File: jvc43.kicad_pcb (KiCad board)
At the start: 6 copper layers, 101.6 x 50.8 mm, 140 parts, among them J201 8P8C_LED_Shielded, J301 8P8C_LED_Shielded, J401 USB_C_Receptacle_USB2.0, U201 LAN8831, U301 LAN8831, U401 LTC3622*DE, X101 25 MHz

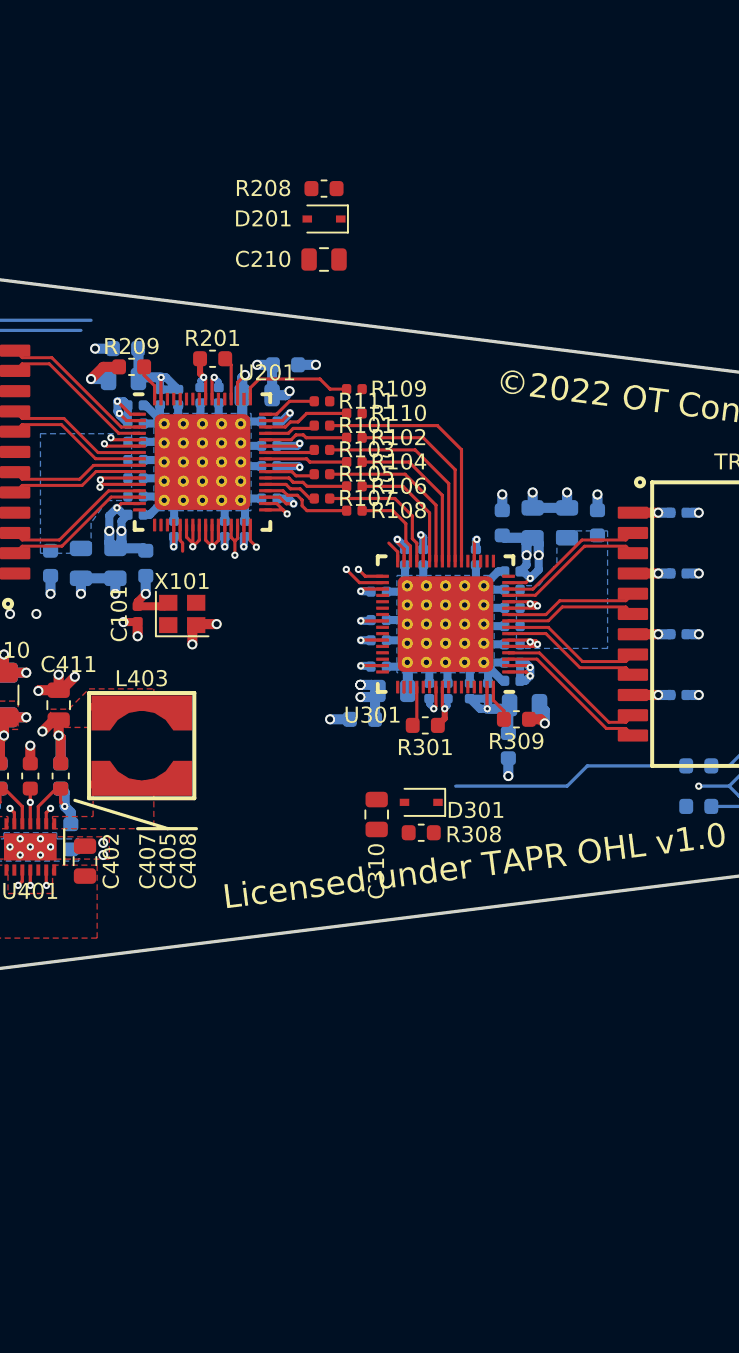
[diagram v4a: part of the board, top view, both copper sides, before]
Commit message: Added the absurd number of config/MODE/PHYAD strap resistors, 16 per PHY !!! They have been added to the layout, but not yet placed or routed.
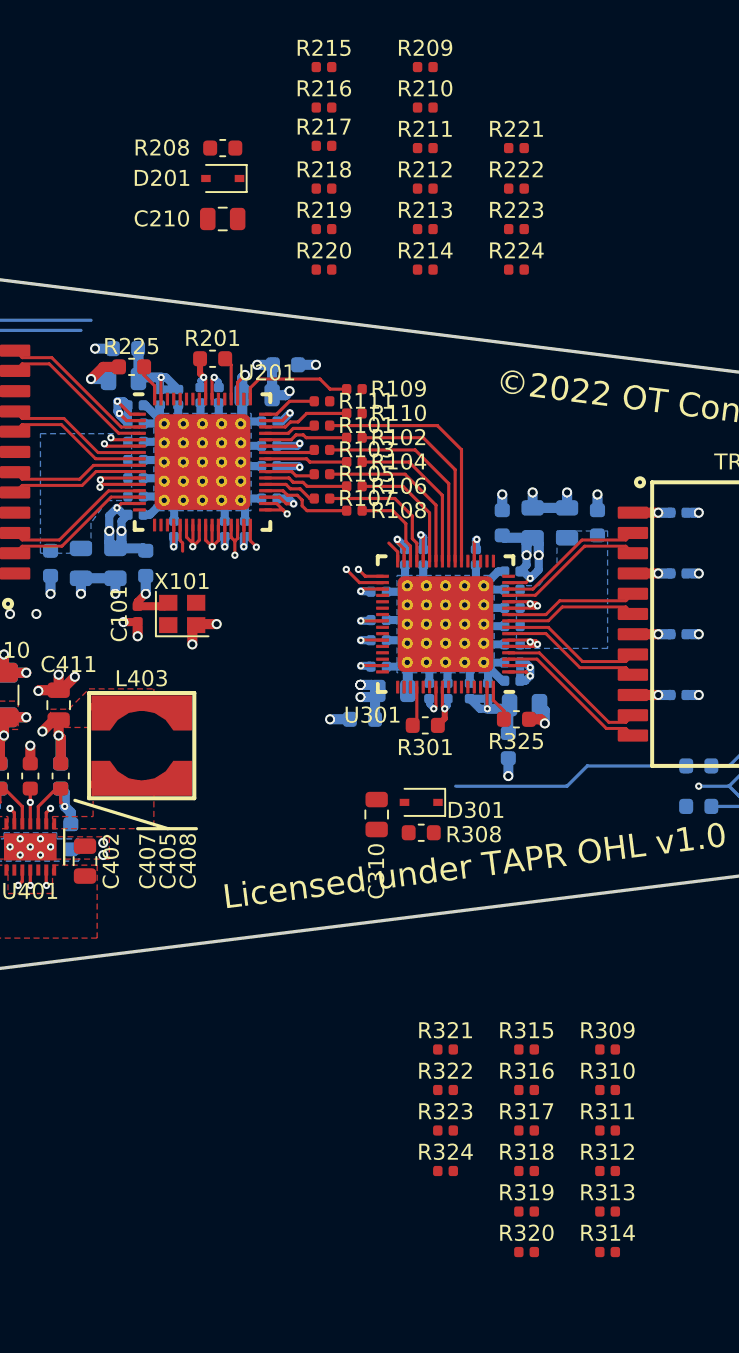
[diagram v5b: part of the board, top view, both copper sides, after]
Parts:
- added R209: 10k, Resistor_SMD:R_0402_1005Metric, F.Cu at (82.5, 15.9)
- added R210: 10k, Resistor_SMD:R_0402_1005Metric, F.Cu at (82.5, 18.4)
- added R211: 10k, Resistor_SMD:R_0402_1005Metric, F.Cu at (82.5, 21.0)
- added R212: 10k, Resistor_SMD:R_0402_1005Metric, F.Cu at (82.5, 23.5)
- added R213: 10k, Resistor_SMD:R_0402_1005Metric, F.Cu at (82.5, 26.0)
- added R214: 10k, Resistor_SMD:R_0402_1005Metric, F.Cu at (82.5, 28.6)
- added R215: 10k, Resistor_SMD:R_0402_1005Metric, F.Cu at (76.2, 15.9)
- added R216: 10k, Resistor_SMD:R_0402_1005Metric, F.Cu at (76.2, 18.4)
- added R217: dnp, Resistor_SMD:R_0402_1005Metric, F.Cu at (76.2, 20.8)
- added R218: 10k, Resistor_SMD:R_0402_1005Metric, F.Cu at (76.2, 23.5)
- added R219: 10k, Resistor_SMD:R_0402_1005Metric, F.Cu at (76.2, 26.0)
- added R220: 10k, Resistor_SMD:R_0402_1005Metric, F.Cu at (76.2, 28.6)
- added R221: 10k, Resistor_SMD:R_0402_1005Metric, F.Cu at (88.3, 21.0)
- added R222: 10k, Resistor_SMD:R_0402_1005Metric, F.Cu at (88.3, 23.5)
- added R223: 10k, Resistor_SMD:R_0402_1005Metric, F.Cu at (88.3, 26.0)
- added R224: 10k, Resistor_SMD:R_0402_1005Metric, F.Cu at (88.3, 28.6)
- added R309: 10k, Resistor_SMD:R_0402_1005Metric, F.Cu at (94.0, 77.5)
- added R310: 10k, Resistor_SMD:R_0402_1005Metric, F.Cu at (94.0, 80.0)
- added R311: 10k, Resistor_SMD:R_0402_1005Metric, F.Cu at (94.0, 82.5)
- added R312: 10k, Resistor_SMD:R_0402_1005Metric, F.Cu at (94.0, 85.1)
- added R313: 10k, Resistor_SMD:R_0402_1005Metric, F.Cu at (94.0, 87.6)
- added R314: 10k, Resistor_SMD:R_0402_1005Metric, F.Cu at (94.0, 90.2)
- added R315: 10k, Resistor_SMD:R_0402_1005Metric, F.Cu at (88.9, 77.5)
- added R316: 10k, Resistor_SMD:R_0402_1005Metric, F.Cu at (88.9, 80.0)
- added R317: dnp, Resistor_SMD:R_0402_1005Metric, F.Cu at (88.9, 82.5)
- added R318: 10k, Resistor_SMD:R_0402_1005Metric, F.Cu at (88.9, 85.1)
- added R319: 10k, Resistor_SMD:R_0402_1005Metric, F.Cu at (88.9, 87.6)
- added R320: 10k, Resistor_SMD:R_0402_1005Metric, F.Cu at (88.9, 90.2)
- added R321: 10k, Resistor_SMD:R_0402_1005Metric, F.Cu at (83.8, 77.5)
- added R322: 10k, Resistor_SMD:R_0402_1005Metric, F.Cu at (83.8, 80.0)
- added R323: 10k, Resistor_SMD:R_0402_1005Metric, F.Cu at (83.8, 82.5)
- added R324: 10k, Resistor_SMD:R_0402_1005Metric, F.Cu at (83.8, 85.1)
- R202, R203, R302, R303: value 100 -> 220
- moved C210 6.84 mm to (69.8, 25.4)
- moved R208 6.84 mm to (69.8, 21.0)
- moved D201 6.84 mm to (69.8, 22.9)
- renumbered R209 to R225, R309 to R325
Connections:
- J201 pad 10: GND -> /Ethernet1/green
- J201 pad 11: /Ethernet1/yellow -> +2V5
- J201 pad 12: GND -> /Ethernet1/yellow
- J201 pad 9: /Ethernet1/green -> +2V5
- J301 pad 10: GND -> /Ethernet2/green
- J301 pad 11: /Ethernet2/yellow -> +2V5
- J301 pad 12: GND -> /Ethernet2/yellow
- J301 pad 9: /Ethernet2/green -> +2V5
- R202 pad 1: /Ethernet1/100_LED -> /Ethernet1/LED1
- R203 pad 1: /Ethernet1/1000_LED -> /Ethernet1/LED2
- R302 pad 1: /Ethernet2/100_LED -> /Ethernet2/LED1
- R303 pad 1: /Ethernet2/1000_LED -> /Ethernet2/LED2
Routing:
- net /Ethernet2/LED1: track 0.00 -> 15.0 mm
- net /Ethernet2/100_LED: track 15.0 -> 0.00 mm
- net /Ethernet1/LED2: track 0.00 -> 13.7 mm
- net /Ethernet1/1000_LED: track 13.7 -> 0.00 mm
- net /Ethernet1/LED1: track 1.70 -> 14.5 mm
- net /Ethernet1/100_LED: track 12.8 -> 0.00 mm

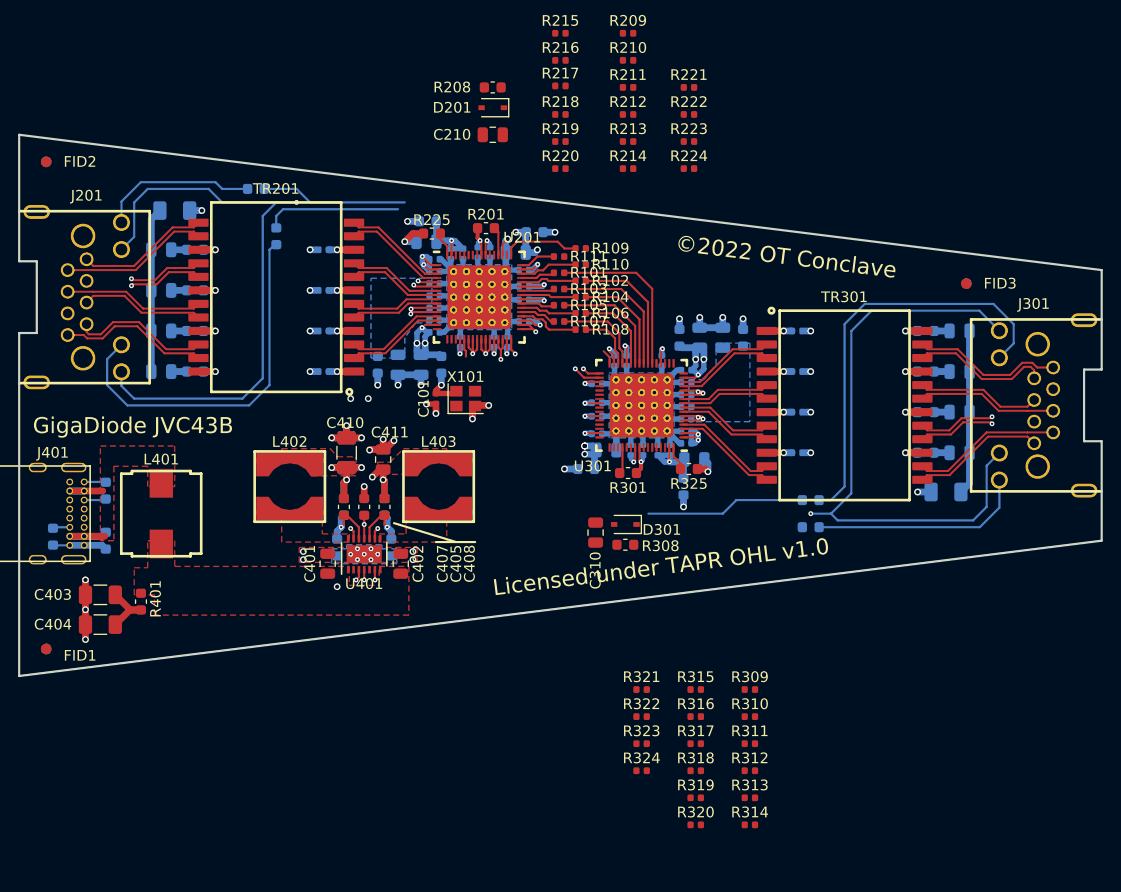
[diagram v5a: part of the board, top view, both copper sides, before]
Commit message: - Fixed a schematic bug, one of the strap resistors was connected to RXD2 but   should have been RXD4 - Swapped out reset 10k resistor from size 0603 to size 0402, since I have now   32 more of them in the smaller size... also assigned a mfr P/N to all those - Placed and routed *EVERYTHING* for PHY2, mainly all the new strap resistors - Placed and routed the new LED traces (both PHYs), and a few of the PHY1   straps, namely the LED1-5 straps
Still to go: place & route of the config & PHYAD strap resistors for PHY1...
It's getting very crowded
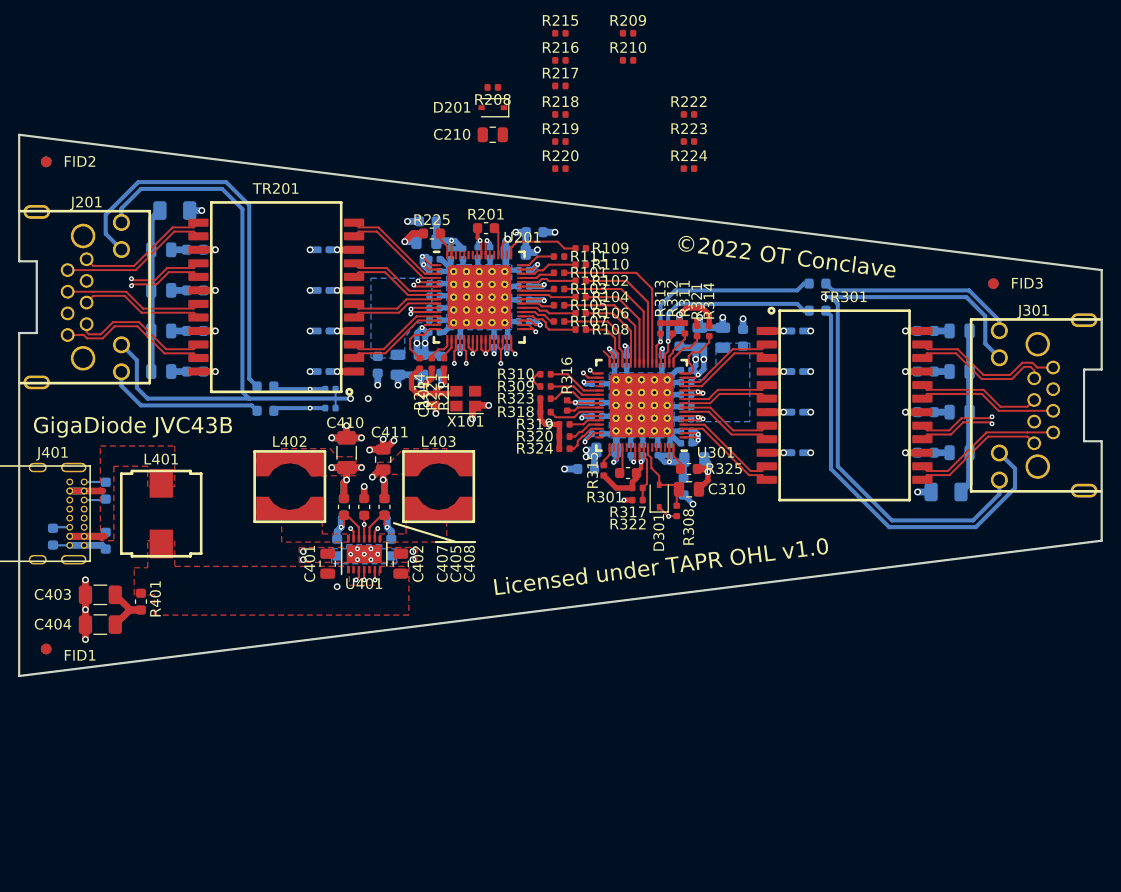
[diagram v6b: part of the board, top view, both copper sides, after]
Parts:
- R208, R308: footprint Resistor_SMD:R_0603_1608Metric -> Resistor_SMD:R_0402_1005Metric
- R212, R213: moved to B.Cu
- moved R314 46.5 mm to (90.2, 43.8), turned to 270 degrees
- moved R313 44.9 mm to (85.6, 43.6), turned to 270 degrees
- moved R312 42.2 mm to (86.7, 43.6), turned to 270 degrees
- moved R311 39.5 mm to (87.9, 43.6), turned to 270 degrees
- moved R320 38.5 mm to (76.6, 53.7), turned to 180 degrees
- moved R212 38.0 mm to (54.6, 49.3), turned to 180 degrees
- moved R213 37.5 mm to (54.6, 51.1), turned to 180 degrees
- moved R310 37.4 mm to (74.8, 47.9)
- moved R319 37.2 mm to (76.6, 52.6), turned to 180 degrees
- moved R318 36.5 mm to (74.8, 51.4), turned to 180 degrees
- moved R221 35.4 mm to (64.1, 46.9), turned to 270 degrees
- moved R309 34.3 mm to (74.8, 49.0)
- moved R321 34.1 mm to (89.0, 43.8), turned to 90 degrees
- moved R323 33.6 mm to (74.8, 50.2), turned to 180 degrees
- moved R316 31.6 mm to (76.8, 50.8), turned to 270 degrees
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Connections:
- R223 pad 1: /RXD2 -> /RXD4
- R323 pad 1: /Ethernet2/RXD2 -> /Ethernet2/RXD4
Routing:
- net +2V5: track 36.7 -> 178.2 mm, vias 16 -> 19
- net GND: track 214.3 -> 119.1 mm, vias 49 -> 50
- net /Ethernet1/green: track 14.8 -> 36.8 mm
- net /Ethernet2/yellow: track 39.3 -> 18.7 mm
- net /Ethernet2/green: track 20.3 -> 40.0 mm
- net /Ethernet1/yellow: track 34.7 -> 15.0 mm
- net /Ethernet2/LED2: track 0.00 -> 19.6 mm, vias 0 -> 1
- net /Ethernet1/LED1: track 14.5 -> 23.8 mm, vias 0 -> 2
- net /Ethernet1/LED2: track 13.7 -> 21.8 mm, vias 0 -> 2
- net /Ethernet2/nRST: track 0.00 -> 7.60 mm
- net /Ethernet2/LED1: track 15.0 -> 21.2 mm, vias 0 -> 1
- net /Ethernet2/LED5: track 0.00 -> 5.58 mm
- net /Ethernet2/CLK125: track 0.00 -> 5.23 mm
- net /Ethernet2/RXD6: track 0.00 -> 5.21 mm
- net /Ethernet2/RXD4: track 0.00 -> 5.10 mm
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
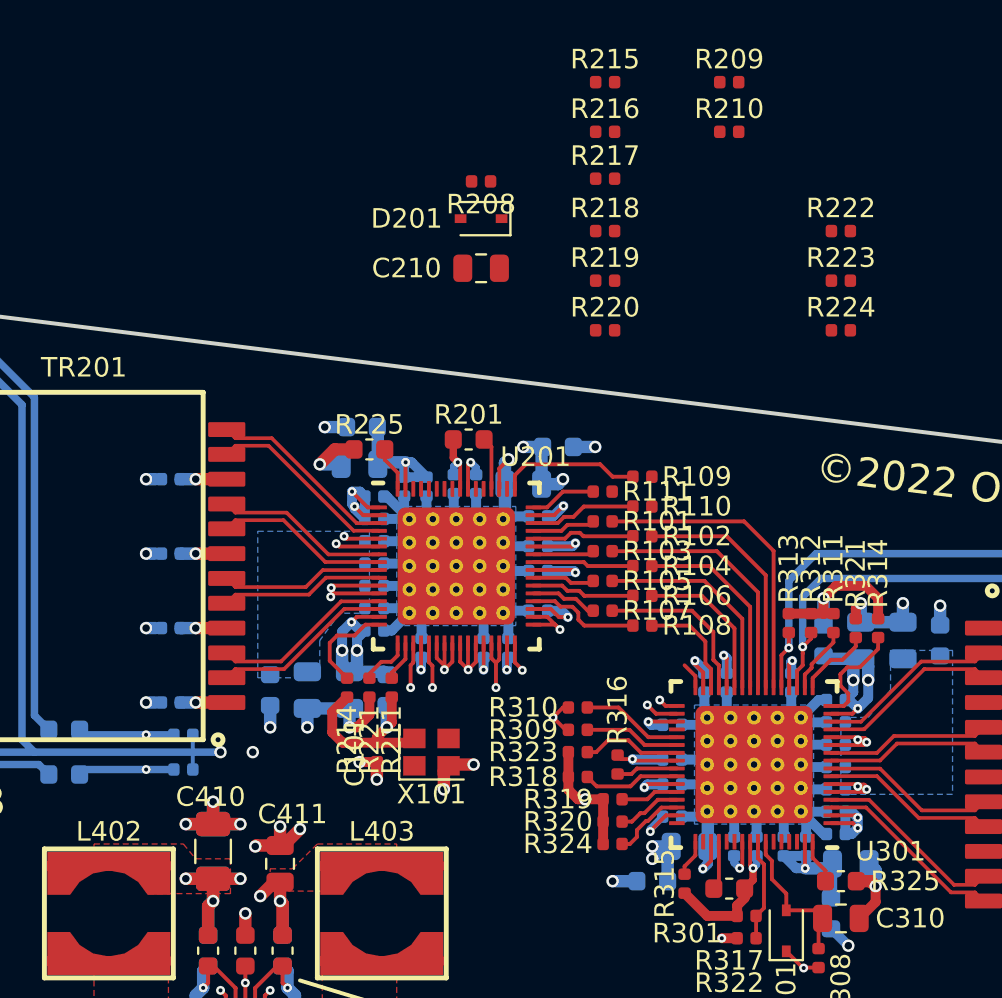
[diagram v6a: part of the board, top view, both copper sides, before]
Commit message: FINISHED all place and route!!! - Moved the 22ohm series resistors to the right 25 mils to make room for vias   on the left column of resistors.  The 10k straps are all then directly   underneath their corresponding series resistors. - Placed the PHY1 reset & option-strap underneath the transformer, because   there was no room left. - Routed the 25 MHz clock trace from the oscillator out to both PHYs, on layer   four.  Had to move the PHY1 VDDAL pour left 25 mils to make room for the   clock trace.
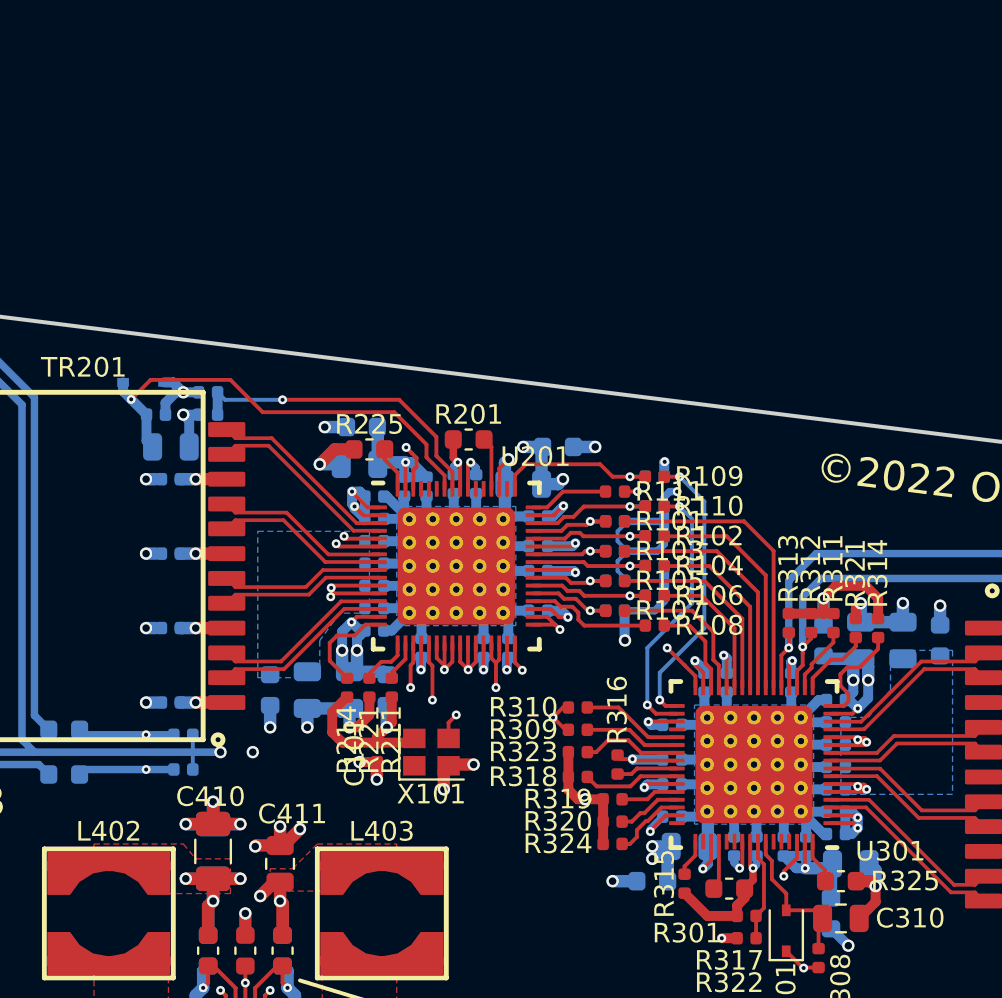
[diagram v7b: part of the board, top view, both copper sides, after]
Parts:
- C210, D201, R208, R209, R210, R215, R216, R217, R218, R219, R220, R222, R223, R224: moved to B.Cu
- moved R222 33.7 mm to (55.9, 32.9), turned to 180 degrees
- moved R209 26.6 mm to (78.7, 42.2), turned to 180 degrees
- moved R210 25.2 mm to (76.7, 42.9), turned to 180 degrees
- moved R217 23.1 mm to (55.9, 31.8)
- moved R216 22.4 mm to (78.7, 40.6), turned to 180 degrees
- moved R208 20.5 mm to (53.2, 32.9)
- moved R215 20.4 mm to (78.7, 36.1), turned to 180 degrees
- moved R223 19.2 mm to (76.7, 41.4)
- moved D201 19.2 mm to (52.6, 31.2)
- moved C210 18.3 mm to (54.0, 34.5)
- moved R218 16.4 mm to (76.7, 39.9)
- moved R219 13.3 mm to (78.7, 39.1)
- moved R224 13.1 mm to (78.7, 37.6)
- moved R220 9.79 mm to (76.7, 38.4)
- moved R101 0.64 mm to (76.7, 38.4)
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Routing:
- net /Ethernet1/XI: track 0.00 -> 44.3 mm, vias 0 -> 3
- net /Ethernet1/nRST: track 0.00 -> 23.5 mm, vias 0 -> 1
- net /Ethernet1/CLK125: track 0.00 -> 16.3 mm, vias 0 -> 1
- net /CLK_W2B: track 1.00 -> 14.7 mm, vias 1 -> 2
- net GND: track 119.1 -> 132.7 mm, vias 50 -> 52
- net /EN_W2B: track 1.70 -> 13.9 mm, vias 1 -> 2
- net /ER_W2B: track 1.36 -> 11.9 mm, vias 0 -> 2
- net +2V5: track 178.2 -> 188.3 mm, vias 19 -> 22
- net /RXD6: track 3.42 -> 4.84 mm, vias 0 -> 1
- net /RXD2: track 3.13 -> 4.55 mm, vias 0 -> 1
- net /RXD4: track 3.21 -> 4.63 mm, vias 0 -> 1
- net /RXD0: track 3.26 -> 4.68 mm, vias 0 -> 1
- net /Ethernet1/RXCLK: track 7.23 -> 8.65 mm, vias 0 -> 1
- net /RXD5: track 5.31 -> 6.73 mm, vias 0 -> 1
- net /RXD3: track 5.17 -> 6.59 mm, vias 0 -> 1
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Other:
- rule trace_min: 0.1778 -> 0.18796
